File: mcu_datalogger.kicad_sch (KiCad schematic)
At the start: 25 parts, among them U1 DS1337S_, U2 ATMEGA328P-AU, U3 24LC1025, U4 24LC1025, Y1 32.768MHz, Y2 16MHz

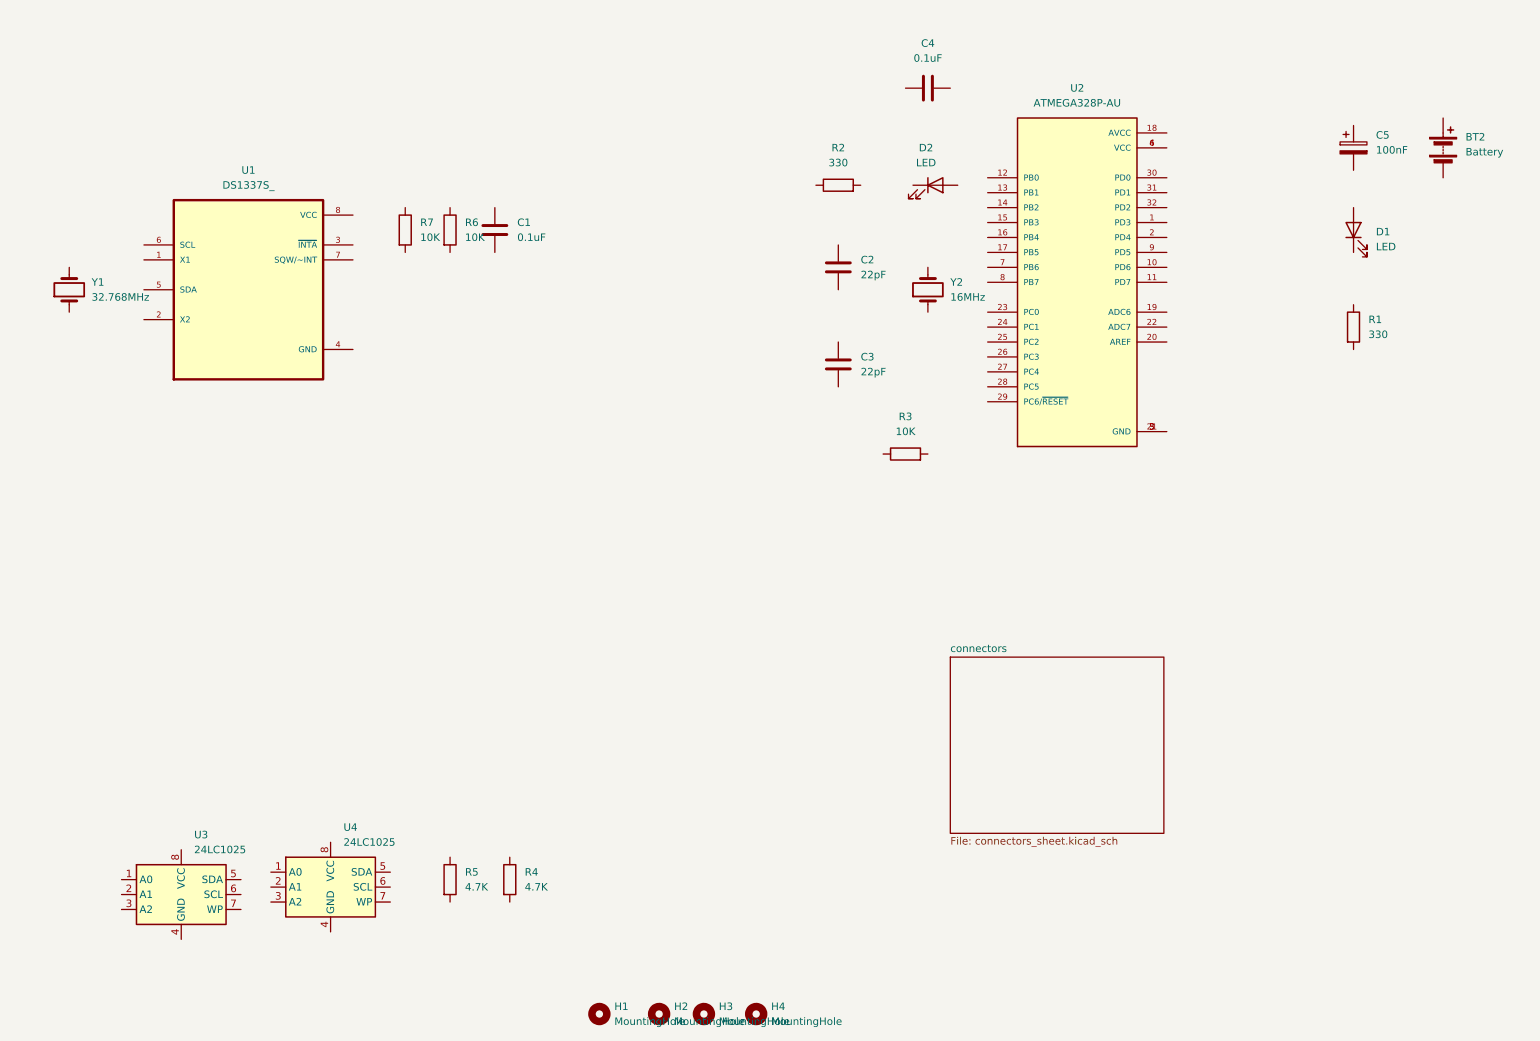
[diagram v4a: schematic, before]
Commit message: Complted the wiring of main sheet
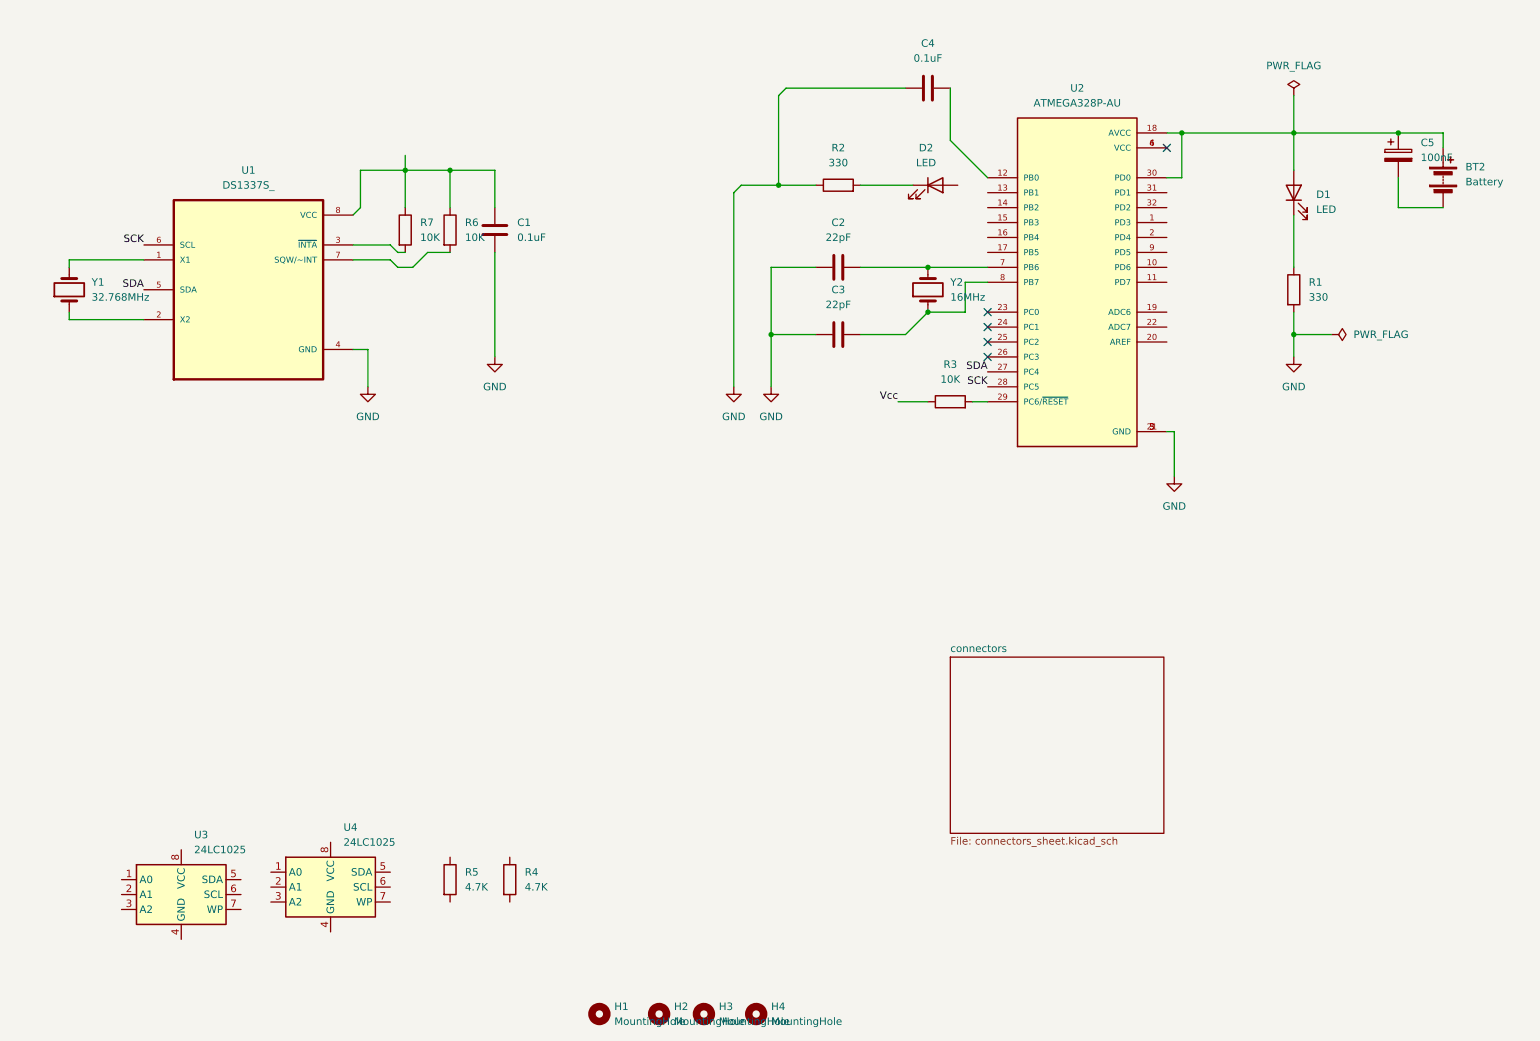
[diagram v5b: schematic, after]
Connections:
- net at D1.1 (K): now also R1.1
- net at D1.2 (A): now also BT2.1 (+), C5.1, U2.18 (AVCC), U2.30 (PD0)
- net at U1.1 (X1): now also Y1.2
- net at U1.2 (X2): now also Y1.1
- net at U1.3 (~{INTA}): now also R7.2
- net GND: now reaches U1.4 (GND)
- net GND: now also C1.2, C2.1, C3.1, C4.1, R1.2, R2.1, U2.21 (GND), U2.3 (GND), U2.5 (GND)
- net SDA: now reaches U1.5 (SDA)
- net SDA: now also U2.27 (PC4)
- net SCK: now reaches U1.6 (SCL)
- net SCK: now also U2.28 (PC5)
- net at U1.7 (SQW/~INT): now also R6.2
- net at U1.8 (VCC): now also C1.1, R6.1, R7.1
- net at R2.2: now also D2.1 (K)
- net at C4.2: now also U2.12 (PB0)
- net at U2.29 (PC6/~{RESET}): now also R3.2
- net at U2.7 (PB6): now also C2.2, Y2.2
- net at U2.8 (PB7): now also C3.2, Y2.1
- net at BT2.2 (-): now also C5.2
- net Vcc: now reaches R3.1
- no-connect marks 0 -> 5
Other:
- moved on the sheet: BT2, C2, C3, C5, D1, R1, R3

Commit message: Added Pin diagram to the Connector
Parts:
- removed U2: ATMEGA328P-AU, ATMEGA328P-AU:QFP80P900X900X120-32N, symbol ATMEGA328P-AU:ATMEGA328P-AU
- added U5: ATMEGA328P-AU, ATMEGA328P-AU:QFP80P900X900X120-32N, symbol ATMEGA328P-AU:ATMEGA328P-AU
- Y1: value 32.768MHz -> 32.768 KHz
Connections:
- net GND: now also BT2.2 (-), C5.2, U3.4 (GND), U3.7 (WP), U4.2 (A1), U4.4 (GND), U4.7 (WP), U5.21 (GND), U5.3 (GND), U5.5 (GND)
- net SCK: now also D2.2 (A), R5.2, U3.6 (SCL), U4.6 (SCL), U5.17 (PB5), U5.28 (PC5)
- net SDA: now also R4.2, U3.5 (SDA), U4.5 (SDA), U5.27 (PC4)
- net Vcc: now also R4.1, R5.1, U3.1 (A0), U3.2 (A1), U3.3 (A2), U3.8 (VCC), U4.1 (A0), U4.3 (A2), U4.8 (VCC)
- net at BT2.1 (+), C5.1, D1.2 (A): now also U5.18 (AVCC), U5.4 (VCC)
- net at C4.2: now also U5.20 (AREF)
- net RESET: now reaches R3.2
- net RESET: now also U5.29 (PC6/~{RESET})
- net at C2.2, Y2.2: now also U5.7 (PB6)
- net at C3.2, Y2.1: now also U5.8 (PB7)
- new net D2: U5.32 (PD2)
- new net D3: U5.1 (PD3)
- new net D4: U5.2 (PD4)
- new net D5: U5.9 (PD5)
- new net D6: U5.10 (PD6)
- new net D7: U5.11 (PD7)
- new net D8: U5.12 (PB0)
- new net MISO: U5.16 (PB4)
- new net MOSI: U5.15 (PB3)
- new net RX: U5.30 (PD0)
- new net TX: U5.31 (PD1)
- no-connect marks 5 -> 3
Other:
- moved on the sheet: BT2, C2, C3, C4, C5, D1, D2, R1, R2, R3, U3, Y2

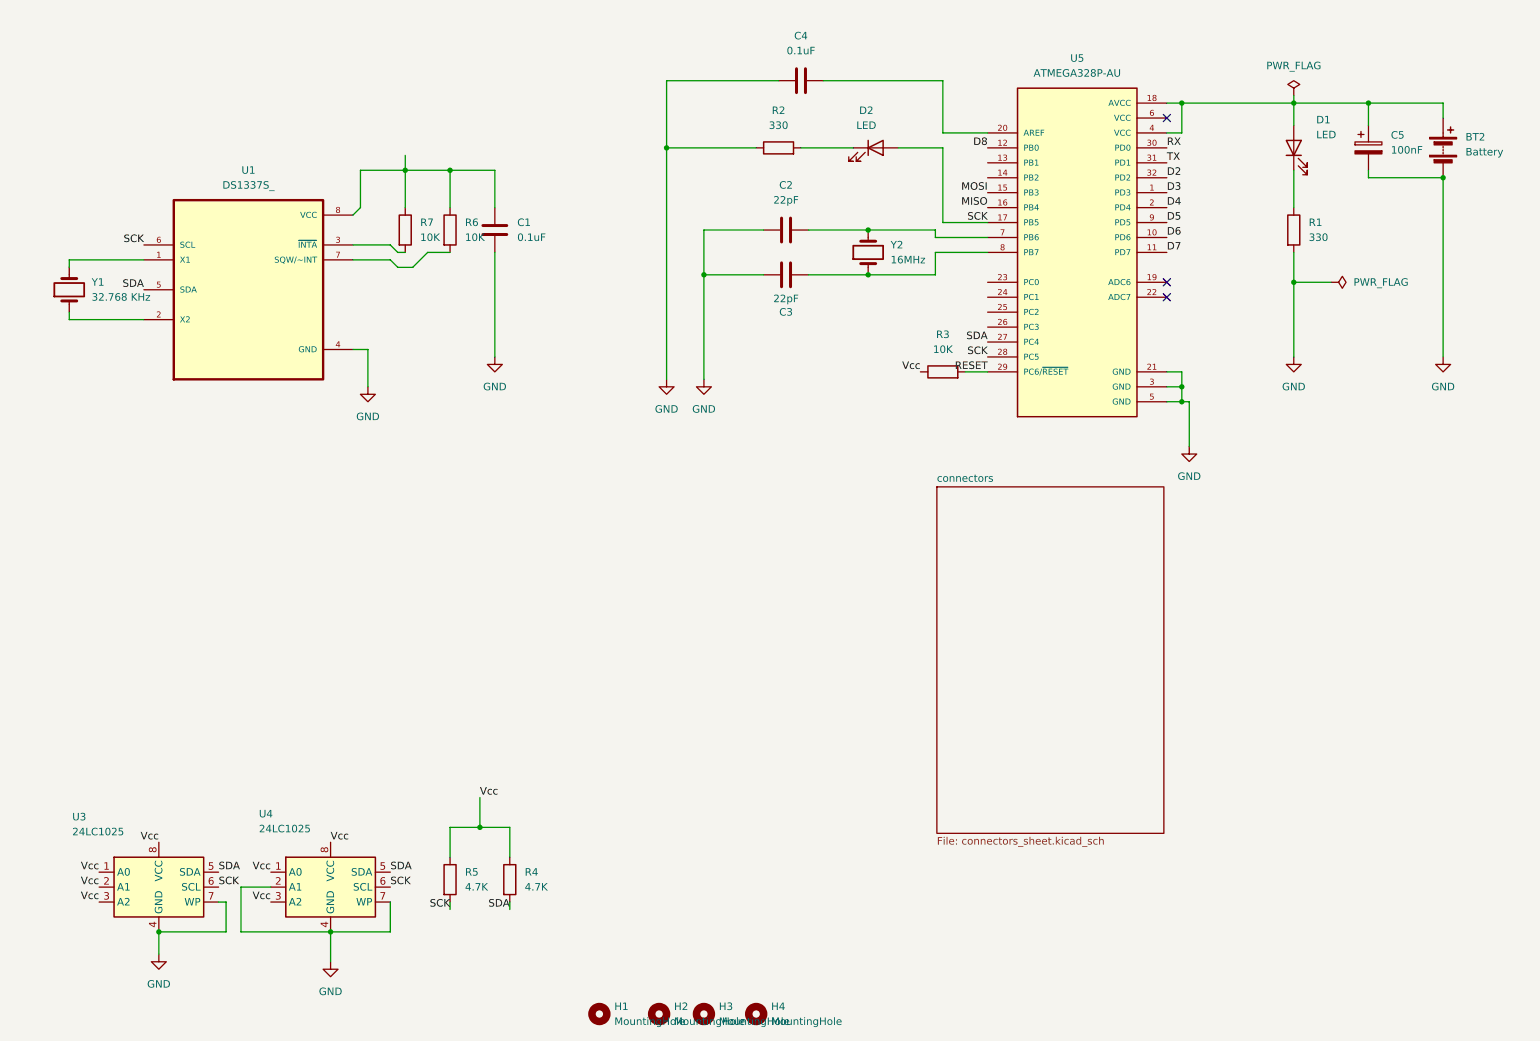
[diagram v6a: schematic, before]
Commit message: Schematic Diagram connections are added
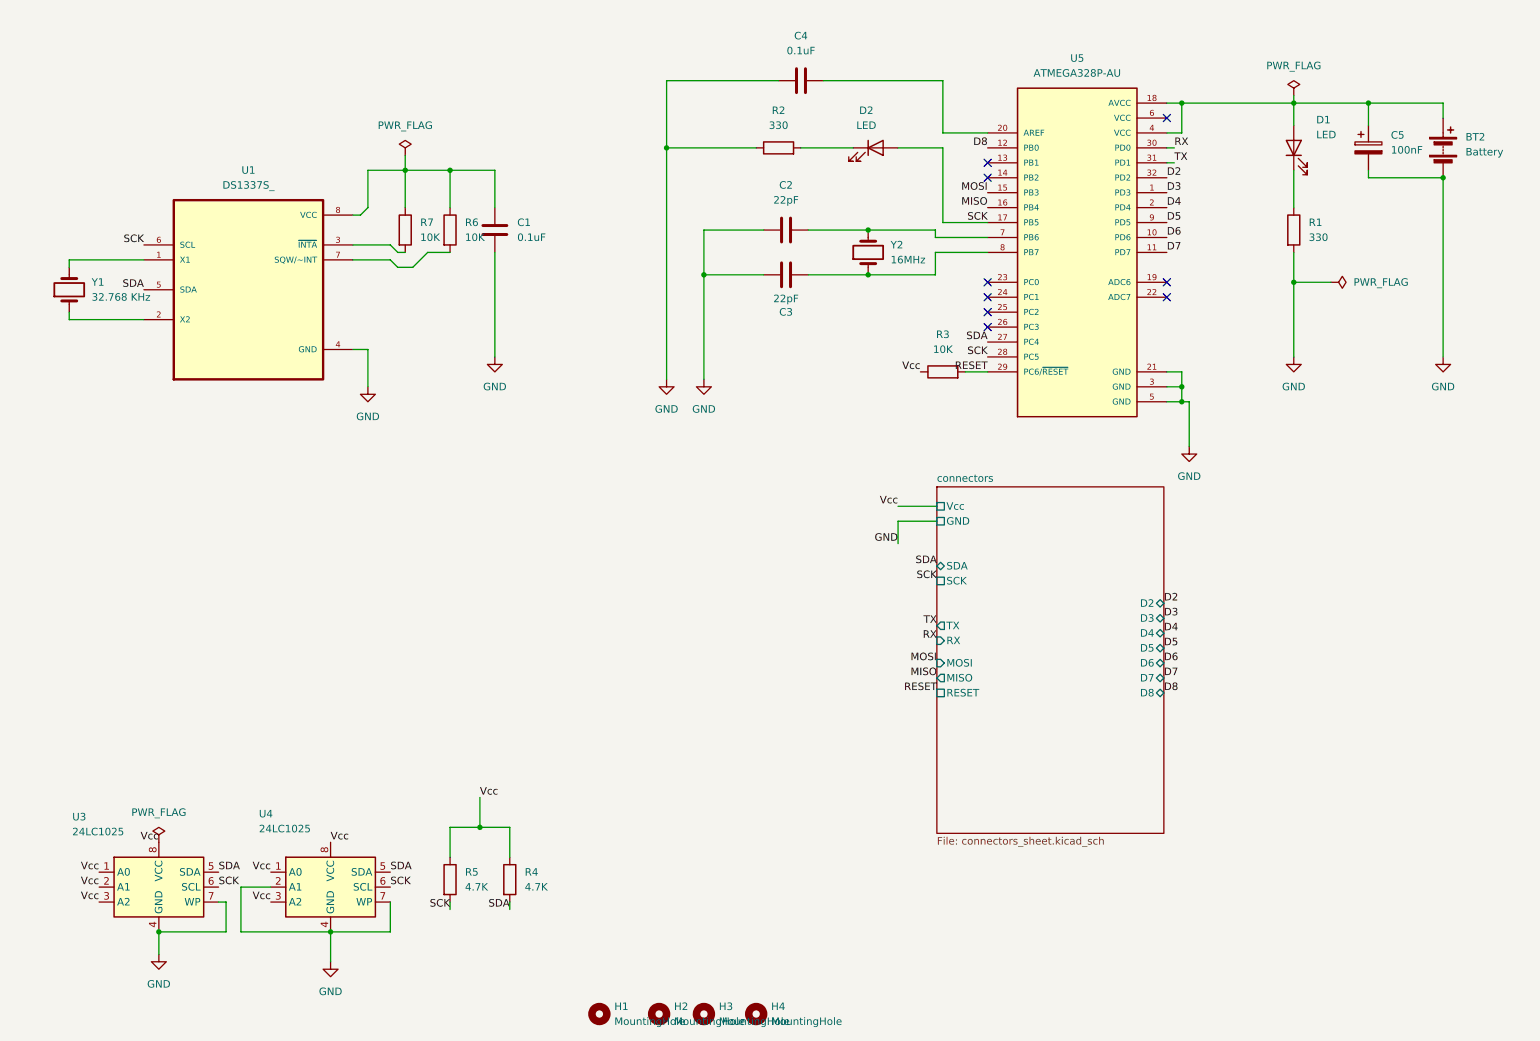
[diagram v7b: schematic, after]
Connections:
- no-connect marks 3 -> 9
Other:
- sheet connectors ports: added D2, D3, D4, D5, D6, D7, D8, GND, MISO, MOSI, RESET, RX, SCK, SDA, TX, Vcc; removed none

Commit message: Added Text &Marking for Easy understanding
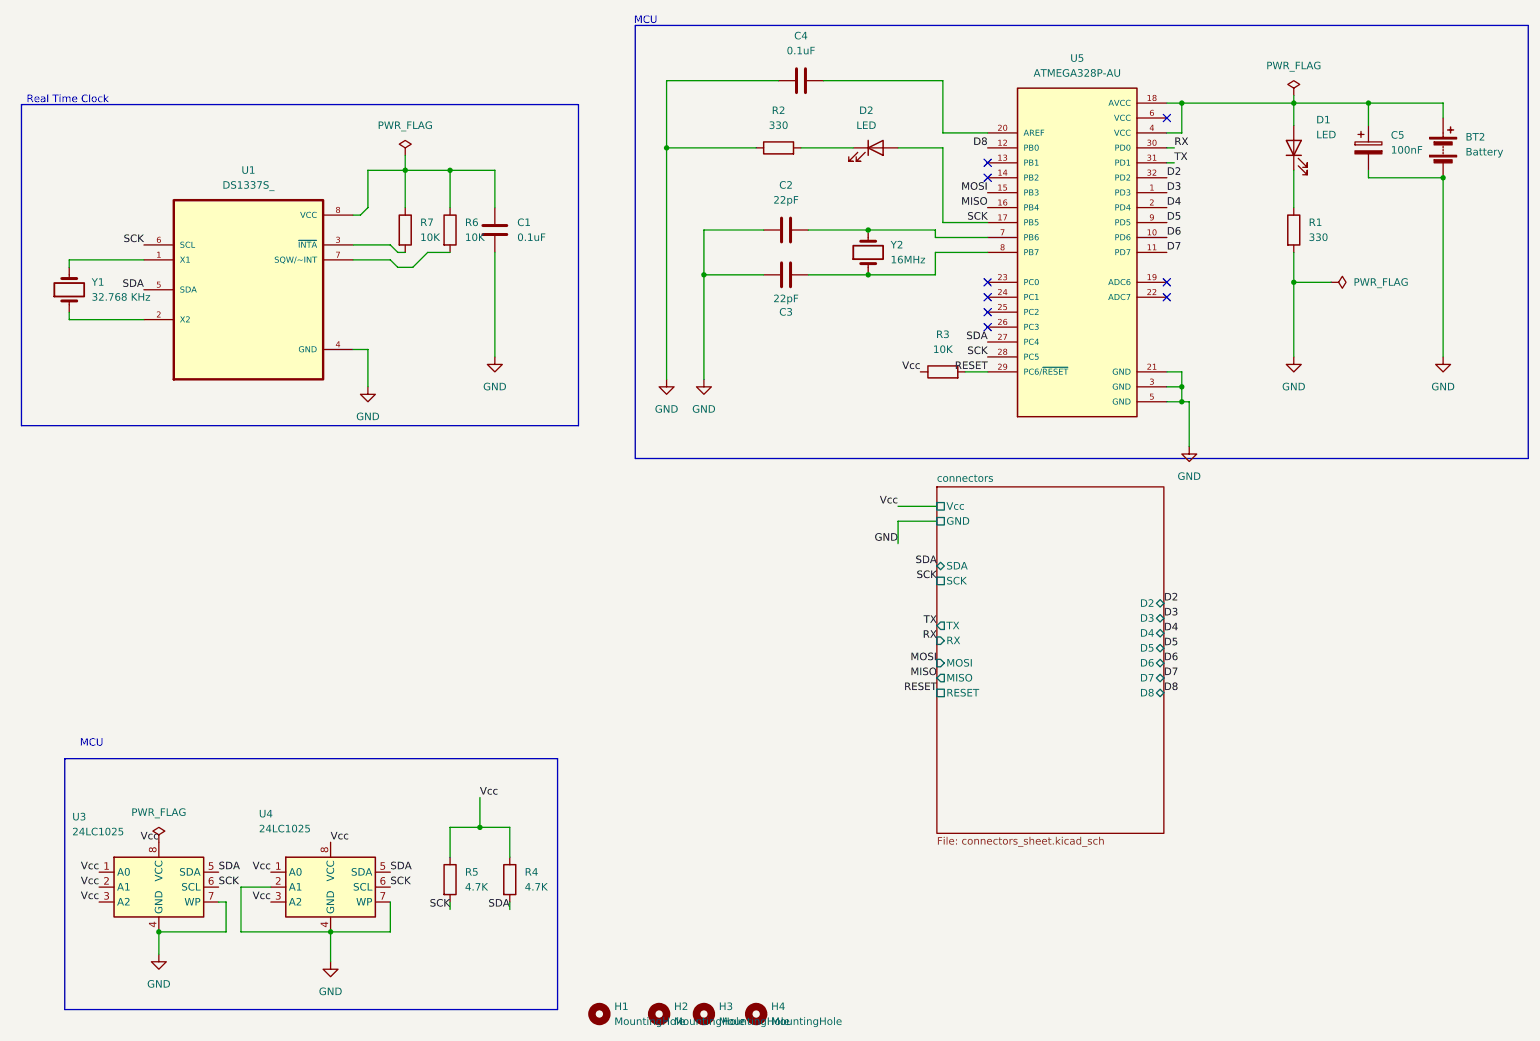
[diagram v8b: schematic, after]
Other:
- note added: "MCU"
- note added: "Real Time Clock"
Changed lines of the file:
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@@
+		)
+	)
+	(rectangle
+		(start 23.622 34.544)
+		(end 118.364 89.154)
+		(stroke
+			(width 0)
+			(type default)
+		)
+		(fill
+			(type none)
+		)
+	)
+	(rectangle
+		(start 128.016 21.082)
+		(end 279.908 94.742)
+		(stroke
+			(width 0)
+			(type default)
+		)
+		(fill
+			(type none)
+		)
+	)
+	(rectangle
+		(start 30.988 145.796)
+		(end 114.808 188.468)
+		(stroke
+			(width 0)
+			(type default)
+		)
+		(fill
+			(type none)
+		)
+	)
+	(text "Real Time Clock\n"
+		(exclude_from_sim no)
+		(at 31.496 33.782 0)
+		(effects
+			(font
+				(size 1.27 1.27)
+			)
+		)
+	)
+	(text "MCU\n"
+		(exclude_from_sim no)
+		(at 35.56 143.256 0)
+		(effects
+			(font
+				(size 1.27 1.27)
+			)
+		)
+	)
+	(text "MCU\n"
+		(exclude_from_sim no)
+		(at 129.794 20.32 0)
+		(effects
+			(font
+				(size 1.27 1.27)
+			)
 		)
 	)
